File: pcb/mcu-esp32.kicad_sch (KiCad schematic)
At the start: 2 parts, among them U8 ESP32-S3-WROOM-1-N8R8

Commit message: Add TPS2121 Stage 2/3: USB-vs-battery priority muxing on 5V and 3.3V rails
power.kicad_sch:
- U14 (TPS2121RUXR): 5V rail mux. IN1=BATT_5V_REG (priority), IN2=USB_5V_IN,
  OUT=+5V. PR1 tied to IN1, CP2/OV1/OV2 to GND (VREF priority mode -- battery
  always wins when present, no voltage-comparison ambiguity between two
  nominally-5V sources). ILM set via R26 (30.1k, ~3.5A class, sized with
  margin above the 2A SA818 budget for TX current transients). SS via C42
  (0.01uF). ST feeds the battery/USB detect logic below.
- U13 (TPS2121RUXR): 3.3V rail mux, same configuration. IN1=BATT_3.3V_REG,
  IN2=USB_3.3V_IN, OUT=+3.3V. ILM via R25 (80.6k, ~1.5A class, vs 1A
  peripheral budget). SS via C41.
- U1 (74LVC1G08): AND-gates U13.ST and U14.ST (each pulled up individually
  via R27/R28, 10k to +3.3V, since ST is open-drain) into PWR_ON_BATTERY --
  high only when both rails are confirmed running from battery, low if
  either has fallen back to USB. Output exposed as a new Power sheet pin.

foxhunt1.kicad_sch: bridges PWR_ON_BATTERY (Power sheet) to the new
IO_IN_ON_BATT input on the mcu-esp32 sheet, and USB_3.3V_IN/USB_5V_IN
(Power sheet) to USB_3.3V/USB_5V (USB-C sheet) -- these were previously
unconnected placeholder labels.

mcu-esp32.kicad_sch: IO_IN_ON_BATT wired to U8 pin 35 (GPIO42), the one
GPIO the pinout doc had marked as still spare.

kicad_gx_library: TPS2121RUXR symbol fix (one OUT pin marked passive
instead of output, since the two physical OUT pins are meant to be tied
together -- avoids an ERC driver-conflict false positive).

power_regulation.kicad_sch, battery_18650_input.kicad_sch,
battery_powerpole_input.kicad_sch, foxhunt1.kicad_pro: incidental KiCad
save cleanup, no circuit changes (verified via orphan/short checks and
netlist diff -- same components as before).

Fully traced pin-by-pin: both mux dividers/ILM/SS wiring, the battery-vs-
USB source assignment on each rail (not swapped), the AND-gate inputs,
and all three cross-sheet bridges. 0 new orpha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
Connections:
- net IO_IN_ON_BATT: now reaches U8.35 (MTMS/GPIO42)
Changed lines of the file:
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@@
+		(color 0 0 0 0)
+	)
+	(junction
+		(at 146.05 62.23)
+		(diameter 0)
 		(color 0 0 0 0)
 	)
@@
 	(wire
 		(pts
+			(xy 146.05 62.23) (xy 146.05 76.2)
+		)
+		(stroke
+			(width 0)
+			(type default)
+		)
+	)
+	(wire
+		(pts
 			(xy 191.77 81.28) (xy 194.31 81.28)
 		)
@@
 	(wire
 		(pts
+			(xy 90.17 104.14) (xy 100.33 104.14)
+		)
+		(stroke
+			(width 0)
+			(type default)
+		)
+	)
+	(wire
+		(pts
 			(xy 96.52 152.4) (xy 100.33 152.4)
 		)
@@
 	(wire
 		(pts
+			(xy 146.05 53.34) (xy 146.05 58.42)
+		)
+		(stroke
+			(width 0)
+			(type default)
+		)
+	)
+	(wire
+		(pts
 			(xy 191.77 88.9) (xy 194.31 88.9)
 		)
@@
 	(wire
 		(pts
-			(xy 146.05 55.88) (xy 146.05 58.42)
-		)
-		(stroke
-			(width 0)
-			(type default)
-		)
-	)
-	(wire
-		(pts
-			(xy 146.05 58.42) (xy 146.05 76.2)
+			(xy 146.05 58.42) (xy 146.05 62.23)
 		)
 		(stroke
@@
 			)
 			(justify left)
+		)
+	)
+	(hierarchical_label "IO_IN_ON_BATT"
+		(shape input)
+		(at 90.17 104.14 180)
+		(effects
+			(font
+				(size 1.27 1.27)
+			)
+			(justify right)
 		)
 	)
@@
 	)
 	(symbol
+		(lib_id "power:+3.3V")
+		(at 146.05 53.34 0)
+		(unit 1)
+		(body_style 1)
+		(exclude_from_sim no)
+		(in_bom yes)
+		(on_board yes)
+		(in_pos_files yes)
+		(dnp no)
+		(fields_autoplaced yes)
+		(property "Reference" "#PWR012"
+			(at 146.05 57.15 0)
+			(hide yes)
+			(show_name no)
+			(do_not_autoplace no)
+			(effects
+				(font
+					(size 1.27 1.27)
+				)
+			)
+		)
+		(property "Value" "+3.3V"
+			(at 146.05 48.26 0)
+			(show_name no)
+			(do_not_autoplace no)
+			(effects
+				(font
+					(size 1.27 1.27)
+				)
+			)
+		)
+		(property "Footprint" ""
+			(at 146.05 53.34 0)
+			(hide yes)
+			(show_name no)
+			(do_not_autoplace no)
+			(effects
+				(font
+					(size 1.27 1.27)
+				)
+			)
+		)
+		(property "Datasheet" ""
+			(at 146.05 53.34 0)
+			(hide yes)
+			(show_name no)
+			(do_not_autoplace no)
+			(effects
+				(font
+					(size 1.27 1.27)
+				)
+			)
+		)
+		(property "Description" "Power symbol creates a global label with name \"+3.3V\""
+			(at 146.05 53.34 0)
+			(hide yes)
+			(show_name no)
+			(do_not_autoplace no)
+			(effects
+				(font
+					(size 1.27 1.27)
+				)
+			)
+		)
+		(pin "1"
+		)
+		(instances
+			(project "foxhunt1"
+				(path "/8399ba4b-9428-480d-8b65-76cf154b97a5/617e4003-f89e-4d51-9dfb-cf31f0818925"
+					(reference "#PWR012")
+					(unit 1)
+				)
+			)
+		)
+	)
+	(symbol
+		(lib_id "power:PWR_FLAG")
+		(at 146.05 62.23 90)
+		(unit 1)
+		(body_style 1)
+		(exclude_from_sim no)
+		(in_bom yes)
+		(on_board yes)
+		(in_pos_files yes)
+		(dnp no)
+		(fields_autoplaced yes)
+		(property "Reference" "#FLG014"
+			(at 144.145 62.23 0)
+			(hide yes)
+			(show_name no)
+			(do_not_autoplace no)
+			(effects
+				(font
+					(size 1.27 1.27)
+				)
+			)
+		)
+		(property "Value" "PWR_FLAG"
+			(at 142.24 62.2299 90)
+			(show_name no)
+			(do_not_autoplace no)
+			(effects
+				(font
+					(size 1.27 1.27)
+				)
+				(justify left)
+			)
+		)
+		(property "Footprint" ""
+			(at 146.05 62.23 0)
+			(hide yes)
+			(show_name no)
+			(do_not_autoplace no)
+			(effects
+				(font
+					(size 1.27 1.27)
+				)
+			)
+		)
+		(property "Datasheet" ""
+			(at 146.05 62.23 0)
+			(hide yes)
+			(show_name no)
+			(do_not_autoplace no)
+			(effects
+				(font
+					(size 1.27 1.27)
+				)
+			)
+		)
+		(property "Description" "Special symbol for telling ERC where power comes from"
+			(at 146.05 62.23 0)
+			(hide yes)
+			(show_name no)
+			(do_not_autoplace no)
+			(effects
+				(font
+					(size 1.27 1.27)
+				)
+			)
+		)
+		(pin "1"
+		)
+		(instances
+			(project "foxhunt1"
+				(path "/8399ba4b-9428-480d-8b65-76cf154b97a5/617e4003-f89e-4d51-9dfb-cf31f0818925"
+					(reference "#FLG014")
+					(unit 1)
+				)
+			)
+		)
+	)
+	(symbol
 		(lib_id "Device:C_Small")
 		(at 152.4 60.96 0)
@@
 					(unit 1)
 				)
-			)
-		)
-	)
-	(symbol
-		(lib_id "power:+3.3V")
-		(at 146.05 55.88 0)
-		(unit 1)
-		(body_style 1)
-		(exclude_from_sim no)
-		(in_bom yes)
-		(on_board yes)
-		(in_pos_files yes)
-		(dnp no)
-		(fields_autoplaced yes)
-		(property "Reference" "#PWR038"
-			(at 146.05 59.69 0)
-			(hide yes)
-			(show_name no)
-			(do_not_autoplace no)
-			(effects
-				(font
-					(size 1.27 1.27)
-				)
-			)
-		)
-		(property "Value" "+3.3V"
-			(at 146.05 50.8 0)
-			(hide yes)
-			(show_name no)
-			(do_not_autoplace no)
-			(effects
-				(font
-					(size 1.27 1.27)
-				)
-			)
-		)
-		(property "Footprint" ""
-			(at 146.05 55.88 0)
-			(hide yes)
-			(show_name no)
-			(do_not_autoplace no)
-			(effects
-				(font
-					(size 1.27 1.27)
-				)
-			)
-		)
-		(property "Datasheet" ""
-			(at 146.05 55.88 0)
-			(hide yes)
-			(show_name no)
-			(do_not_autoplace no)
-			(effects
-				(font
-					(size 1.27 1.27)
-				)
-			)
-		)
-		(property "Description" "Power symbol creates a global label with name \"+3.3V\""
-			(at 146.05 55.88 0)
-			(hide yes)
-			(show_name no)
-			(do_not_autoplace no)
-			(effects
-				(font
-					(size 1.27 1.27)
-				)
-			)
-		)
-		(pin "1"
-		)
-		(instances
-			(project "foxhunt1"
-				(path "/8399ba4b-9428-480d-8b65-76cf154b97a5/617e4003-f89e-4d51-9dfb-cf31f0818925"
-					(reference "#PWR038")
-					(unit 1)
-				)

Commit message: Full re-annotation, BOM audit fixes, Stage-1 ILM resize, and PCB reset
Schematic: re-annotated reference designators project-wide (3rd pass) --
every real component's designator has shifted since the last commit.
Fixed BOM gaps found by the fresh audit: U13 (CH340C) sourcing fields,
R7's Manf typo (YAGE -> YAGEO), R5/R8/R14 missing LCSC Part#s, and
normalized U1/U2/U3 (TPS2121RUXR) field names from easyeda2kicad's
defaults (Manufacturer/LCSC Part) to this project's convention
(Manf/LCSC Part #). Resized Stage 1's ILM resistor (R8) from 51.1k to
30.1k -- the prior value undersized the current limit for carrying both
downstream rails' combined battery-side current.

pcb/foxhunt1.kicad_pcb: cleared all footprints. No board layout has
started yet; this reflects that accurately rather than carrying stale
placements from before the schematic settled.

_agent_tasks/bom_property_audit.md: new reusable playbook for this BOM
audit (method, standing exceptions, reporting format), so future passes
don't have to re-derive the approach each time.

_docs/sourcing/task1_lcsc_crossreference.md: replaced stale results
(referencing pre-renumbering designators) with the current audit's
findings. One open item remains: the current-sense shunt's footprint
implies Vishay pad geometry but the sourced part is Milliohm-brand,
needs physical verification before fab.

Co-Authored-By: Claude Sonnet 5 <noreply@anthropic.com>
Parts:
- renumbered C47 to C30, U8 to U10
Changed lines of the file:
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@@
 		(dnp no)
 		(fields_autoplaced yes)
-		(property "Reference" "#PWR037"
+		(property "Reference" "#PWR063"
 			(at 146.05 168.91 0)
 			(hide yes)
@@
 			(project "foxhunt1"
 				(path "/8399ba4b-9428-480d-8b65-76cf154b97a5/617e4003-f89e-4d51-9dfb-cf31f0818925"
-					(reference "#PWR037")
+					(reference "#PWR063")
 					(unit 1)
 				)
@@
 		(dnp no)
 		(fields_autoplaced yes)
-		(property "Reference" "U8"
+		(property "Reference" "U10"
 			(at 148.1933 73.66 0)
 			(show_name no)
@@
 			(project "foxhunt1"
 				(path "/8399ba4b-9428-480d-8b65-76cf154b97a5/617e4003-f89e-4d51-9dfb-cf31f0818925"
-					(reference "U8")
+					(reference "U10")
 					(unit 1)
 				)
@@
 		(dnp no)
 		(fields_autoplaced yes)
-		(property "Reference" "#PWR012"
+		(property "Reference" "#PWR062"
 			(at 146.05 57.15 0)
 			(hide yes)
@@
 			(project "foxhunt1"
 				(path "/8399ba4b-9428-480d-8b65-76cf154b97a5/617e4003-f89e-4d51-9dfb-cf31f0818925"
-					(reference "#PWR012")
+					(reference "#PWR062")
 					(unit 1)
 				)
@@
 		(dnp no)
 		(fields_autoplaced yes)
-		(property "Reference" "#FLG014"
+		(property "Reference" "#FLG018"
 			(at 144.145 62.23 0)
 			(hide yes)
@@
 			(project "foxhunt1"
 				(path "/8399ba4b-9428-480d-8b65-76cf154b97a5/617e4003-f89e-4d51-9dfb-cf31f0818925"
-					(reference "#FLG014")
+					(reference "#FLG018")
 					(unit 1)
 				)
@@
 		(dnp no)
 		(fields_autoplaced yes)
-		(property "Reference" "C47"
+		(property "Reference" "C30"
 			(at 154.94 59.6899 0)
 			(show_name no)
@@
 			(project "foxhunt1"
 				(path "/8399ba4b-9428-480d-8b65-76cf154b97a5/617e4003-f89e-4d51-9dfb-cf31f0818925"
-					(reference "C47")
+					(reference "C30")
 					(unit 1)
 				)
@@
 		(dnp no)
 		(fields_autoplaced yes)
-		(property "Reference" "#PWR039"
+		(property "Reference" "#PWR064"
 			(at 152.4 72.39 0)
 			(hide yes)
@@
 			(project "foxhunt1"
 				(path "/8399ba4b-9428-480d-8b65-76cf154b97a5/617e4003-f89e-4d51-9dfb-cf31f0818925"
-					(reference "#PWR039")
+					(reference "#PWR064")
 					(unit 1)
 				)

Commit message: Add VRAW soft-latch power switch and MCU/RTC wake network
- Q5 (AO3407A P-FET) gates VRAW into Power Regulation, gate driven by
  a shared active-low wake node (button SW3, RTC_PWR_INTERRUPT,
  MCU_OUT_PWR_LATCH) pulled up to VRAW through 1M R29
- Q6 (BSS138) on the mcu-esp32 sheet lets GPIO48 hold the latch from
  a 3.3V-safe domain without exposing the MCU to VRAW voltage
- JP5/JP6 bench-isolation jumpers in the VRAW-gated path, bridged via
  new VRAW_GATED net label into Power Regulation's PWR_IN_SELECT
- JP24 lets USB be excluded from the TPS2121 power muxes for bench
  testing the sleep/wake cycle while still connected over USB-C
- Added blank Peripherals sheet (mcu-esp32 child) with RTC-facing
  pins stubbed and wired at the root, ready for the PCF8563 circuit
- regulation.md updated for the final 6.67V/4.78V intermediate
  voltages and matched-tolerance thin-film feedback dividers
- open_items.md: added power-off path as a follow-up (latch only
  handles power-on today)

Co-Authored-By: Claude Sonnet 5 <noreply@anthropic.com>
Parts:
- added Q6: BSS138, Package_TO_SOT_SMD:SOT-23, symbol Transistor_FET:BSS138
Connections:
- net GND: now also Q6.2 (S)
- net at U10.25 (GPIO48/SPICLK_N/SUBSPICLK_N_DIFF): now also Q6.1 (G)
- net MCU_IN_RTC_INT_ALARM: now reaches U10.39 (GPIO1/TOUCH1/ADC1_CH0)
- new net MCU_OUT_LATCH_EN_OUTPUT: Q6.3 (D)

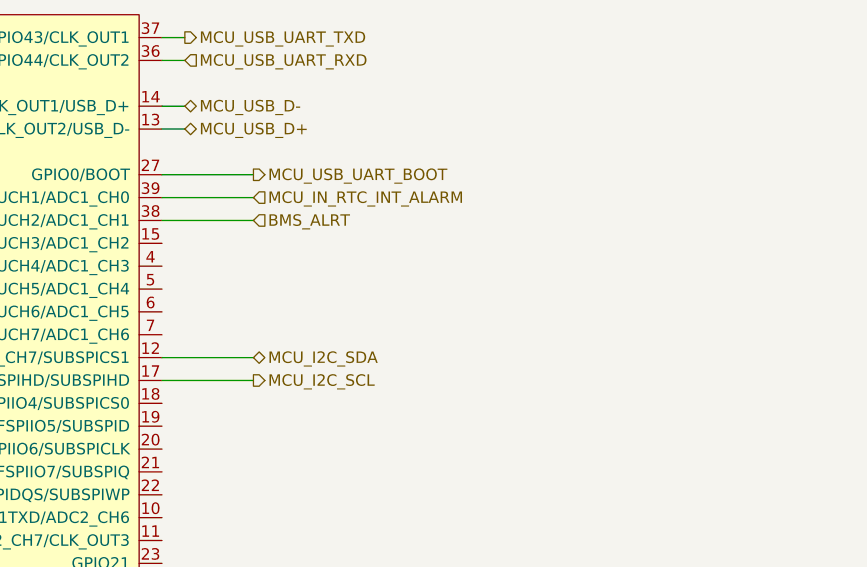
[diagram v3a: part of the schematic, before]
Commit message: Build out PCF8563 RTC peripheral circuit and wire into VRAW latch/MCU
- U14 (PCF8563T) with NDK 9pF crystal (Y2) and DNP OSCI trim cap (C43)
- Coin-cell backup diode-OR: D2/D3 (BAS116) commoned into VDD, BT3
  (CR2032) as backup source, main 3.3V rail as primary
- INT -> Q8 (AO3407A, 3.3V-domain inverter) -> Q7 (BSS138, voltage-safe
  level shift) -> RTC_OUT_INTERRUPT_LATCH, with R31 gate pull-down so
  Q7 has a defined off-state; preserves active-low assert sense onto
  the shared VRAW latch wake node
- R32/R33 (10k) I2C pull-ups on the shared SDA/SCL bus (mcu-esp32,
  Peripherals, and the fuel gauge on Power all share one bus/pull-up
  pair)
- Bump kicad_gx_library for the vendored BAS116LT1G symbol/footprint

Co-Authored-By: Claude Sonnet 5 <noreply@anthropic.com>
Claude-Session: https://claude.ai/code/session_01LhLkuH6sQ5GbUZ61bG7p2h
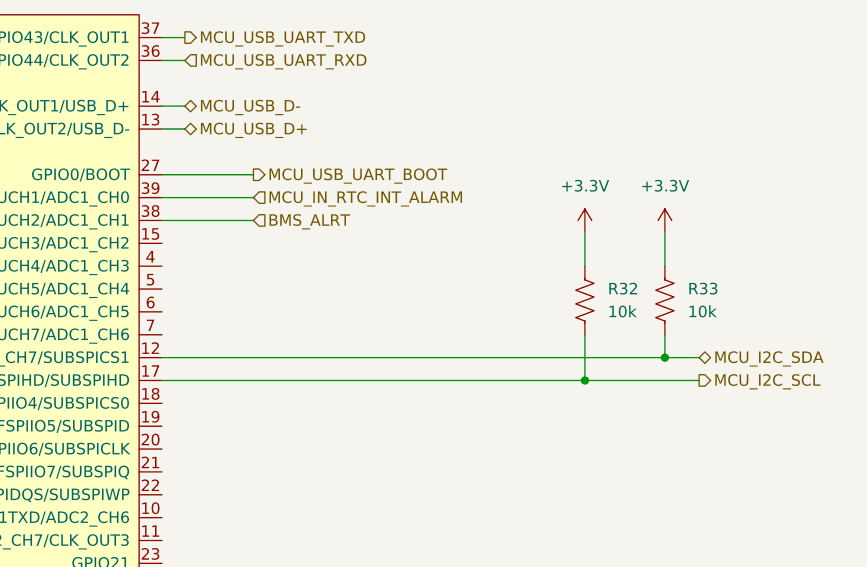
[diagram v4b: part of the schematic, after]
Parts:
- added R32, R33: 10k, Resistor_SMD:R_0603_1608Metric, symbol Device:R_US
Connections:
- net +3.3V: now also R32.2, R33.2
- net MCU_I2C_SCL: now also R32.1
- net MCU_I2C_SDA: now also R33.1

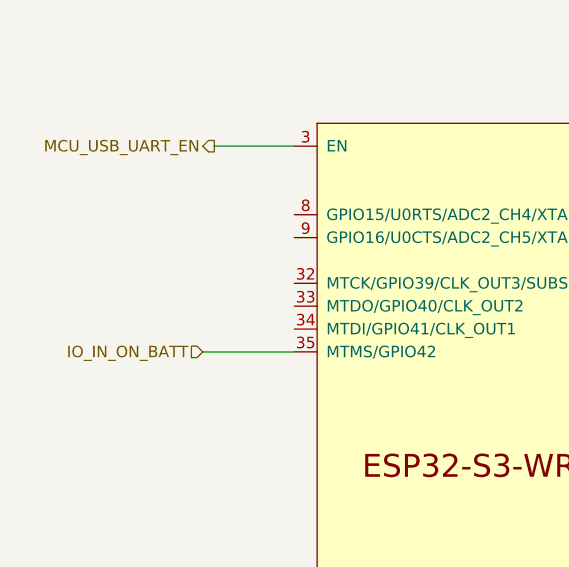
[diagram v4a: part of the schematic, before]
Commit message: Wire up PCA9555 expansion IO section, source LEDs/resistors, swap 3.3V LDO to LM1117
- PCA9555PW expansion IO: DIP switch (SW4, IO0_0-3), onboard buttons
  (SW7-10), status LEDs (D7-10) with sourced series resistors, external
  JST breakouts (J4-7/R39-42) for IO0_4-7, INT pull-up (R34), VDD bypass
  (C49), address pins grounded (addr 0x20)
- Route PCA9555 INT (PERIPH_IO_INT) across the Power/mcu-esp32 top-level
  sheets to the ESP32-S3 (MCU_IN_IO_INT)
- Source real YAGEO MPN/LCSC part numbers for R30/R31/R34-R42
- Fix D10 LED (was orange 0603 with an LCSC part# that resolved to a
  different, wrong part) -> yellow 0805 APTD2012LSYCK, verified Vf/LCSC
  match, matching D7-9's package family
- Fix stale copy-pasted Datasheet links on D7-9 and R31/R35
- Swap 3.3V LDO from AMS1117-3.3 to TI LM1117IMPX-3.3/NOPB (5V LDO swap
  from LM1085IS-5.0 still pending)

Co-Authored-By: Claude Sonnet 5 <noreply@anthropic.com>
Claude-Session: https://claude.ai/code/session_01LhLkuH6sQ5GbUZ61bG7p2h
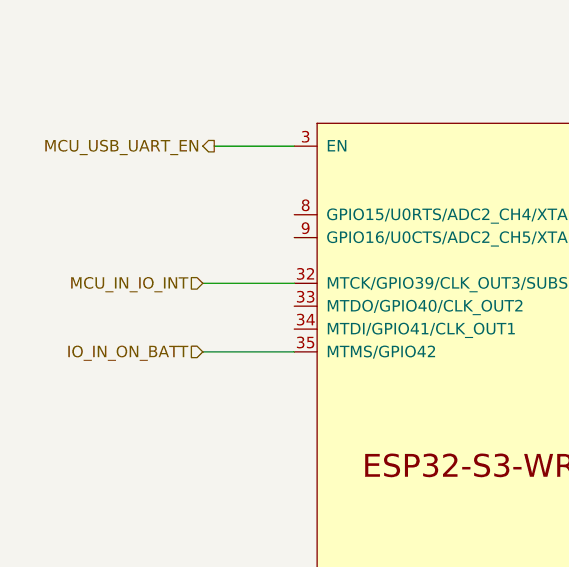
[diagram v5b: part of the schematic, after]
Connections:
- net MCU_IN_IO_INT: now reaches U10.32 (MTCK/GPIO39/CLK_OUT3/SUBSPICS1)
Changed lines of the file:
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@@
+	(wire
+		(pts
+			(xy 90.17 96.52) (xy 100.33 96.52)
+		)
+		(stroke
+			(width 0)
+			(type default)
+		)
+	)
 	(wire
 		(pts
@@
 		)
 	)
+	(hierarchical_label "MCU_IN_IO_INT"
+		(shape input)
+		(at 90.17 96.52 180)
+		(effects
+			(font
+				(size 1.27 1.27)
+			)
+			(justify right)
+		)
+	)
